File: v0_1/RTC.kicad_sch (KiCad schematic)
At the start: 1 part, among them U2 PCF8523T

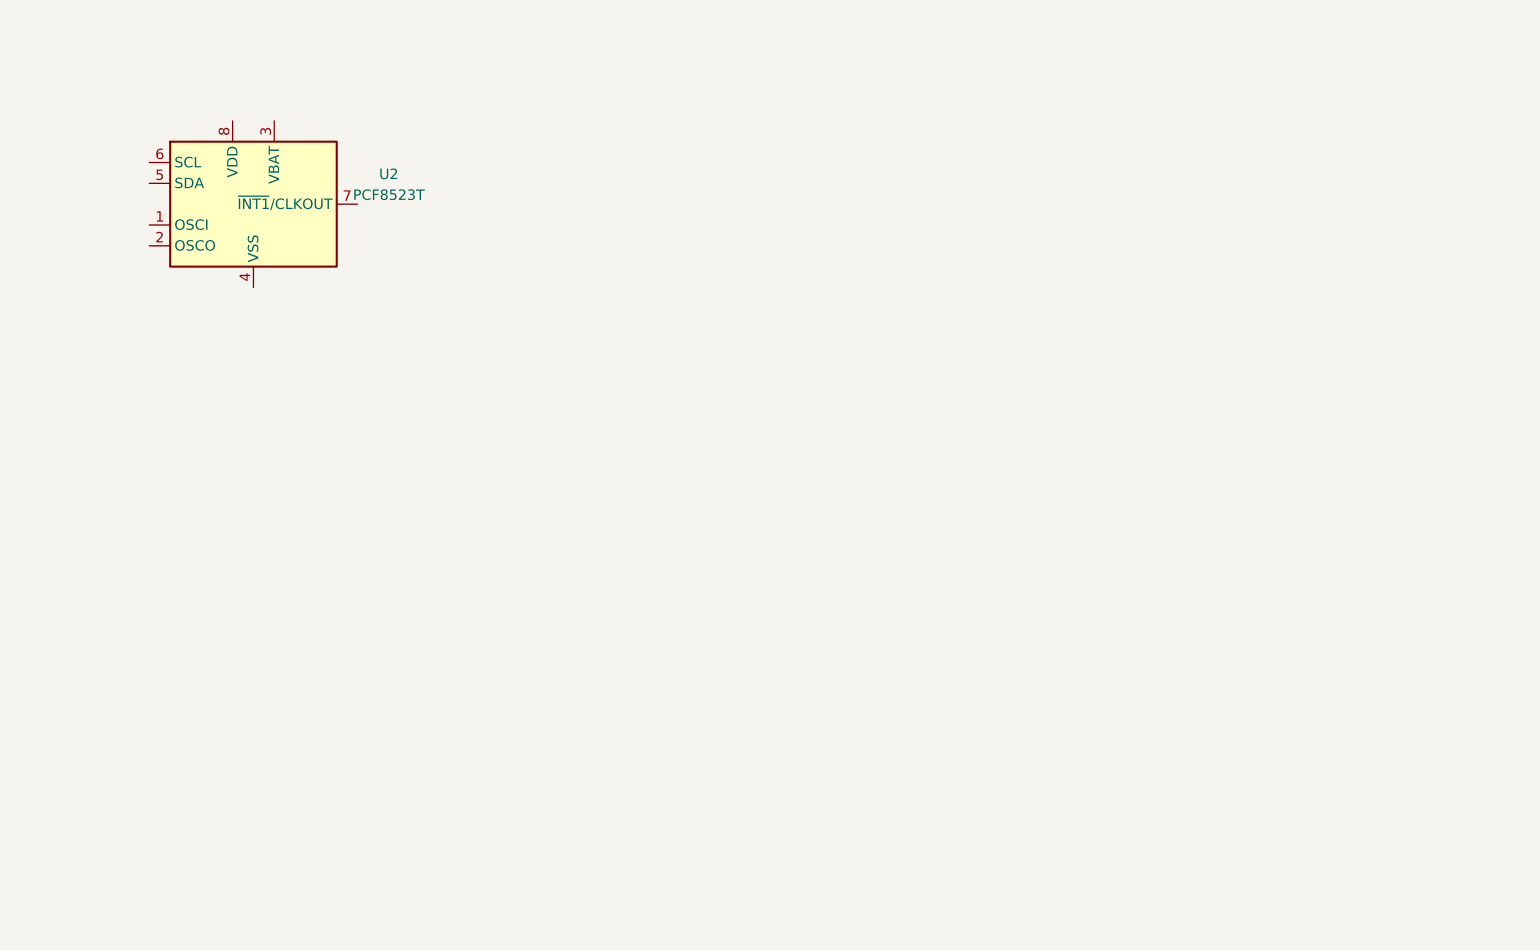
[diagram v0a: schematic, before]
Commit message: add battery case
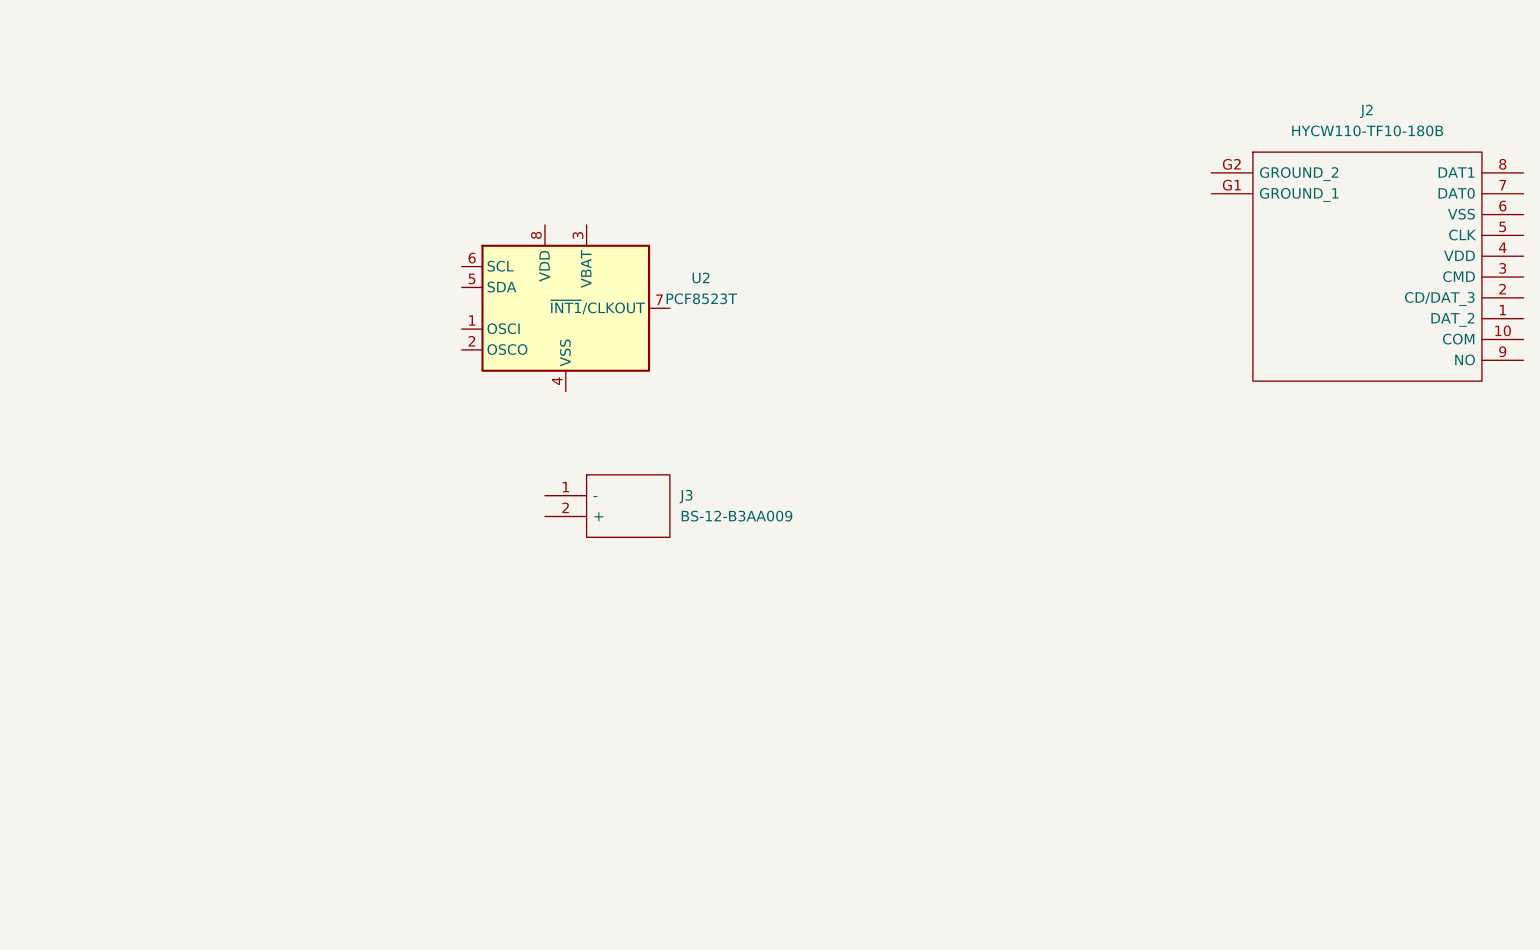
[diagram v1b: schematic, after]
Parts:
- added J2: HYCW110-TF10-180B, HYCW110-TF10-180B:HYCW110TF10180B, symbol HYCW110-TF10-180B:HYCW110-TF10-180B
- added J3: BS-12-B3AA009, BS-12-B3AA009:BS12B3AA009, symbol BS-12-B3AA009:BS-12-B3AA009
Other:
- moved on the sheet: U2
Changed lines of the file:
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@@
 (kicad_sch (version 20230121) (generator eeschema)
   (paper "A4")
-  (symbol (lib_id "Timer_RTC:PCF8523T") (at 91.44 69.85 0) (unit 1)
+  (symbol (lib_id "Timer_RTC:PCF8523T") (at 129.54 82.55 0) (unit 1)
     (in_bom yes) (on_board yes) (dnp no) (fields_autoplaced)
-    (property "Reference" "U2" (at 107.95 66.2021 0)
+    (property "Reference" "U2" (at 146.05 78.9021 0)
       (effects (font (size 1.27 1.27)))
     )
-    (property "Value" "PCF8523T" (at 107.95 68.7421 0)
+    (property "Value" "PCF8523T" (at 146.05 81.4421 0)
       (effects (font (size 1.27 1.27)))
     )
-    (property "Footprint" "Package_SO:SOIC-8_3.9x4.9mm_P1.27mm" (at 111.76 78.74 0)
+    (property "Footprint" "Package_SO:SOIC-8_3.9x4.9mm_P1.27mm" (at 149.86 91.44 0)
       (effects (font (size 1.27 1.27)) hide)
     )
-    (property "Datasheet" "https://www.nxp.com/docs/en/data-sheet/PCF8523.pdf" (at 91.44 69.85 0)
+    (property "Datasheet" "https://www.nxp.com/docs/en/data-sheet/PCF8523.pdf" (at 129.54 82.55 0)
       (effects (font (size 1.27 1.27)) hide)
     )
@@
         )
       )
+    )
+  )
+  (symbol (lib_id "BS-12-B3AA009:BS-12-B3AA009") (at 127 105.41 0) (unit 1)
+    (in_bom yes) (on_board yes) (dnp no) (fields_autoplaced)
+    (property "Reference" "J3" (at 143.51 105.41 0)
+      (effects (font (size 1.27 1.27)) (justify left))
+    )
+    (property "Value" "BS-12-B3AA009" (at 143.51 107.95 0)
+      (effects (font (size 1.27 1.27)) (justify left))
+    )
+    (property "Footprint" "BS-12-B3AA009:BS12B3AA009" (at 143.51 102.87 0)
+      (effects (font (size 1.27 1.27)) (justify left) hide)
+    )
+    (property "Datasheet" "https://datasheet.lcsc.com/lcsc/2012311834_MYOUNG-BS-12-B3AA009_C964727.pdf" (at 143.51 105.41 0)
+      (effects (font (size 1.27 1.27)) (justify left) hide)
+    )
+    (property "Description" "CR1220 SMD Battery Connectors ROHS" (at 143.51 107.95 0)
+      (effects (font (size 1.27 1.27)) (justify left) hide)
+    )
+    (property "Height" "5" (at 143.51 110.49 0)
+      (effects (font (size 1.27 1.27)) (justify left) hide)
+    )
+    (property "Manufacturer_Name" "MYOUNG" (at 143.51 113.03 0)
+      (effects (font (size 1.27 1.27)) (justify left) hide)
+    )
+    (property "Manufacturer_Part_Number" "BS-12-B3AA009" (at 143.51 115.57 0)
+      (effects (font (size 1.27 1.27)) (justify left) hide)
+    )
+    (property "Mouser Part Number" "" (at 143.51 118.11 0)
+      (effects (font (size 1.27 1.27)) (justify left) hide)
+    )
+    (property "Mouser Price/Stock" "" (at 143.51 120.65 0)
+      (effects (font (size 1.27 1.27)) (justify left) hide)
+    )
+    (property "Arrow Part Number" "" (at 143.51 123.19 0)
+      (effects (font (size 1.27 1.27)) (justify left) hide)
+    )
+    (property "Arrow Price/Stock" "" (at 143.51 125.73 0)
+      (effects (font (size 1.27 1.27)) (justify left) hide)
+    )
+    (pin "1")
+    (pin "2")
+    (instances
+      (project "v0_1"
+        (path "/0bf090f4-b9b7-437f-9e6a-e818f47752ec/c334fda6-3f85-41e4-9411-844c140fc2fb"
+          (reference "J3") (unit 1)
+        )
+      )
+    )
+  )
+  (symbol (lib_id "HYCW110-TF10-180B:HYCW110-TF10-180B") (at 208.28 66.04 0) (unit 1)
+    (in_bom yes) (on_board yes) (dnp no) (fields_autoplaced)
+    (property "Reference" "J2" (at 227.33 58.42 0)
+      (effects (font (size 1.27 1.27)))
+    )
+    (property "Value" "HYCW110-TF10-180B" (at 227.33 60.96 0)
+      (effects (font (size 1.27 1.27)))
+    )
+    (property "Footprint" "HYCW110-TF10-180B:HYCW110TF10180B" (at 242.57 63.5 0)
+      (effects (font (size 1.27 1.27)) (justify left) hide)
+    )
+    (property "Datasheet" "https://datasheet.lcsc.com/lcsc/2201241630_HOAUC-HYCW110-TF10-180B_C2962030.pdf" (at 242.57 66.04 0)
+      (effects (font (size 1.27 1.27)) (justify left) hide)
+    )
+    (property "Description" "1A Straight Square Pins 1mm 3.9mm -40~{+105} 1 2.3mm 50 1.27mm Black Brass 1x50P Straight,P=1.27mm Pin Headers ROHS " (at 242.57 68.58 0)
+      (effects (font (size 1.27 1.27)) (justify left) hide)
+    )
+    (property "Height" "2.25" (at 242.57 71.12 0)
+      (effects (font (size 1.27 1.27)) (justify left) hide)
+    )
+    (property "Manufacturer_Name" "HOAUC" (at 242.57 73.66 0)
+      (effects (font (size 1.27 1.27)) (justify left) hide)
+    )
+    (property "Manufacturer_Part_Number" "HYCW110-TF10-180B" (at 242.57 76.2 0)
+      (effects (font (size 1.27 1.27)) (justify left) hide)
+    )
+    (property "Mouser Part Number" "" (at 242.57 78.74 0)
+      (effects (font (size 1.27 1.27)) (justify left) hide)
+    )
+    (property "Mouser Price/Stock" "" (at 242.57 81.28 0)
+      (effects (font (size 1.27 1.27)) (justify left) hide)
+    )
+    (property "Arrow Part Number" "" (at 242.57 83.82 0)
+      (effects (font (size 1.27 1.27)) (justify left) hide)
+    )
+    (property "Arrow Price/Stock" "" (at 242.57 86.36 0)
+      (effects (font (size 1.27 1.27)) (justify left) hide)
+    )
+    (pin "1")
+    (pin "10")
+    (pin "2")
+    (pin "3")
+    (pin "4")
+    (pin "5")
+    (pin "6")
+    (pin "7")
+    (pin "8")
+    (pin "9")
+    (pin "G1")
+    (pin "G2")
+    (instances
+      (project "v0_1"
+        (path "/0bf090f4-b9b7-437f-9e6a-e818f47752ec/c334fda6-3f85-41e4-9411-844c140fc2fb"
+          (reference "J2") (unit 1)
+        )
+      )

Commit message: add rtc and charger schematic
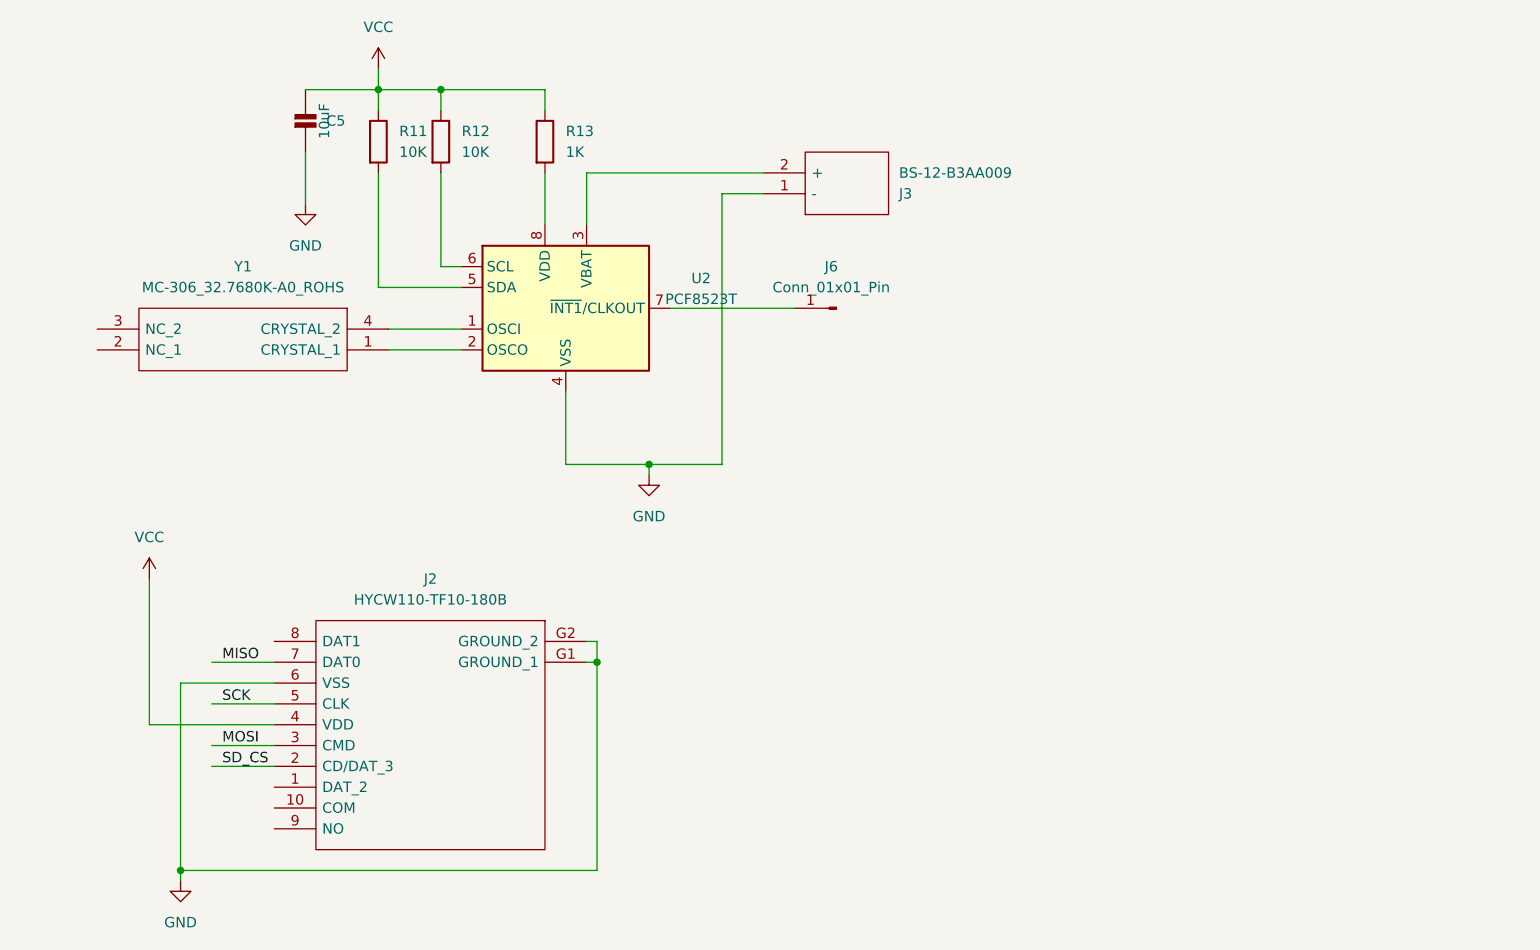
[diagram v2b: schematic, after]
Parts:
- added C5: 10uF, v0_1:_0603, symbol v0_1-eagle-import:CAP_CERAMIC_0603
- added J6: Conn_01x01_Pin, symbol Connector:Conn_01x01_Pin
- added R11, R12: 10K, symbol Device:R
- added R13: 1K, symbol Device:R
- added Y1: MC-306_32.7680K-A0_ROHS, MC-306_32.7680K-A0ROHS:MC306327680KA5ROHS, symbol MC-306_32.7680K-A0_ROHS:MC-306_32.7680K-A0_ROHS
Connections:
- net at U2.1 (OSCI): now also Y1.4 (CRYSTAL_2)
- net at U2.2 (OSCO): now also Y1.1 (CRYSTAL_1)
- net at U2.3 (VBAT): now also J3.2 (+)
- net GND: now reaches U2.4 (VSS)
- net GND: now also J2.6 (VSS), J2.G1 (GROUND_1), J2.G2 (GROUND_2), J3.1 (-), C5.2
- net at U2.5 (SDA): now also R11.2
- net at U2.6 (SCL): now also R12.2
- net at U2.7 (~{INT1}/CLKOUT): now also J6.1 (Pin_1)
- net at U2.8 (VDD): now also R13.2
- net SD_CS: now reaches J2.2 (CD/DAT_3)
- net MOSI: now reaches J2.3 (CMD)
- net VCC: now reaches J2.4 (VDD)
- net VCC: now also C5.1, R11.1, R12.1, R13.1
- net SCK: now reaches J2.5 (CLK)
- net MISO: now reaches J2.7 (DAT0)
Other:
- moved on the sheet: J2, J3

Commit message: add 0.2V
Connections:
- net SDA: now reaches R11.2, U2.5 (SDA)
- net SCL: now reaches R12.2, U2.6 (SCL)
- net VCC renamed +3.3V
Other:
- moved on the sheet: Y1
